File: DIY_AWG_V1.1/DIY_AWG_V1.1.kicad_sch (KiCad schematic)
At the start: 0 parts

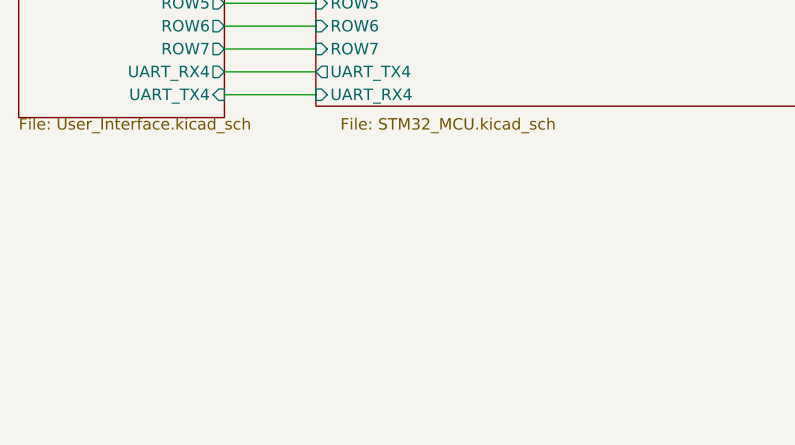
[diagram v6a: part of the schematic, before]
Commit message: Updated PCB design, uploaded necessary footprints and symbols for some components
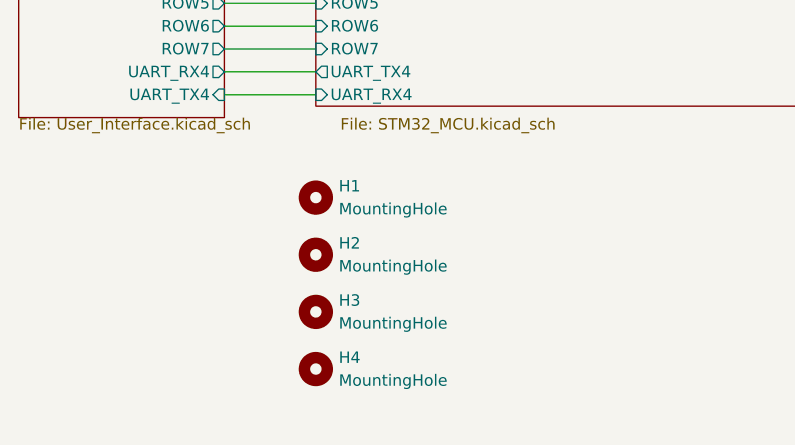
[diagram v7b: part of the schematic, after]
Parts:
- added H1, H2, H3, H4: MountingHole, MountingHole:MountingHole_3.2mm_M3, symbol Mechanical:MountingHole
